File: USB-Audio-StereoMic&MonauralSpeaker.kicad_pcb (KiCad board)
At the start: 2 copper layers, 40 x 40 mm, 39 parts, among them J1 S4B-PH, J2 SJ-2523-SMT-TR, J3 SJ-2523-SMT-TR, J4 S2B-XH-A, J5 SJ2-3593D-SMT-TR, U1 USBLC6-2P6, U2 AP7365-33WG-7, U3 PCM2906CDBR, U4 TPA2006D1DRBR, Y1 12MHz33pF

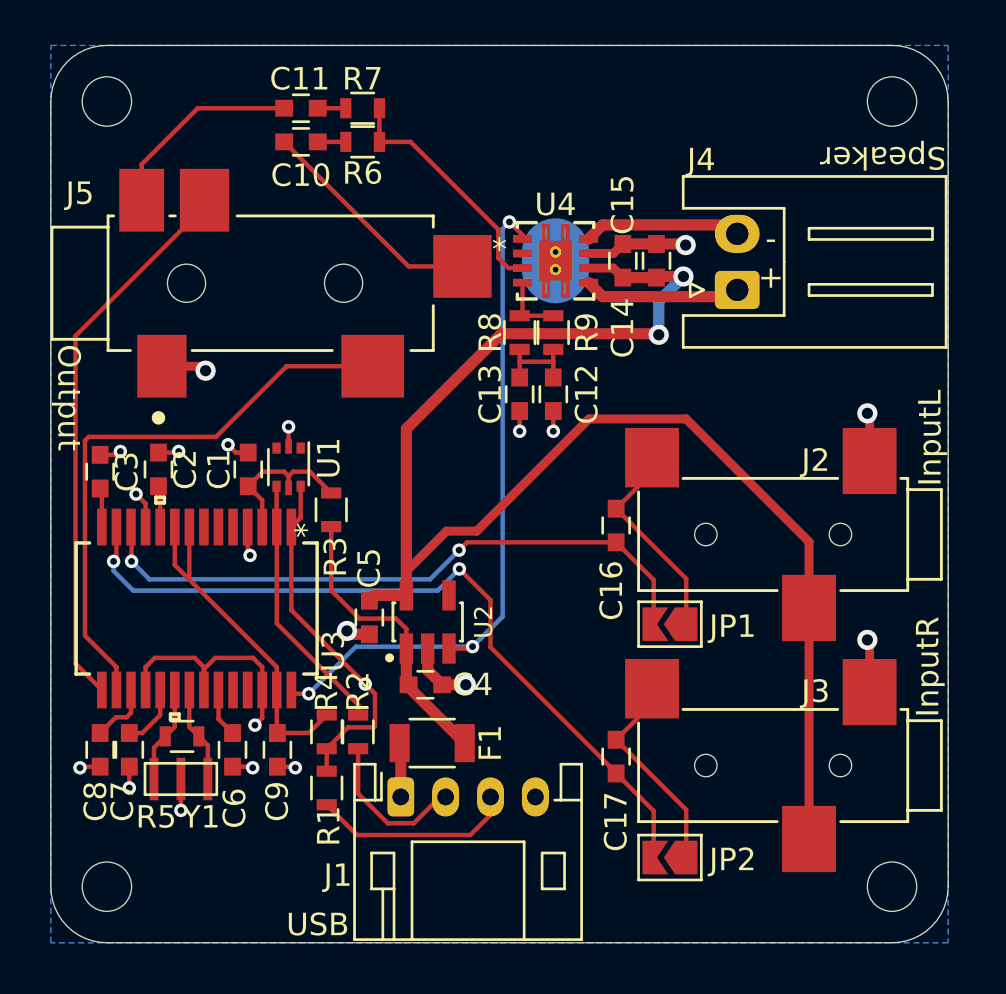
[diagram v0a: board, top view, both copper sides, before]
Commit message: 市販のモノラルマイクに対応
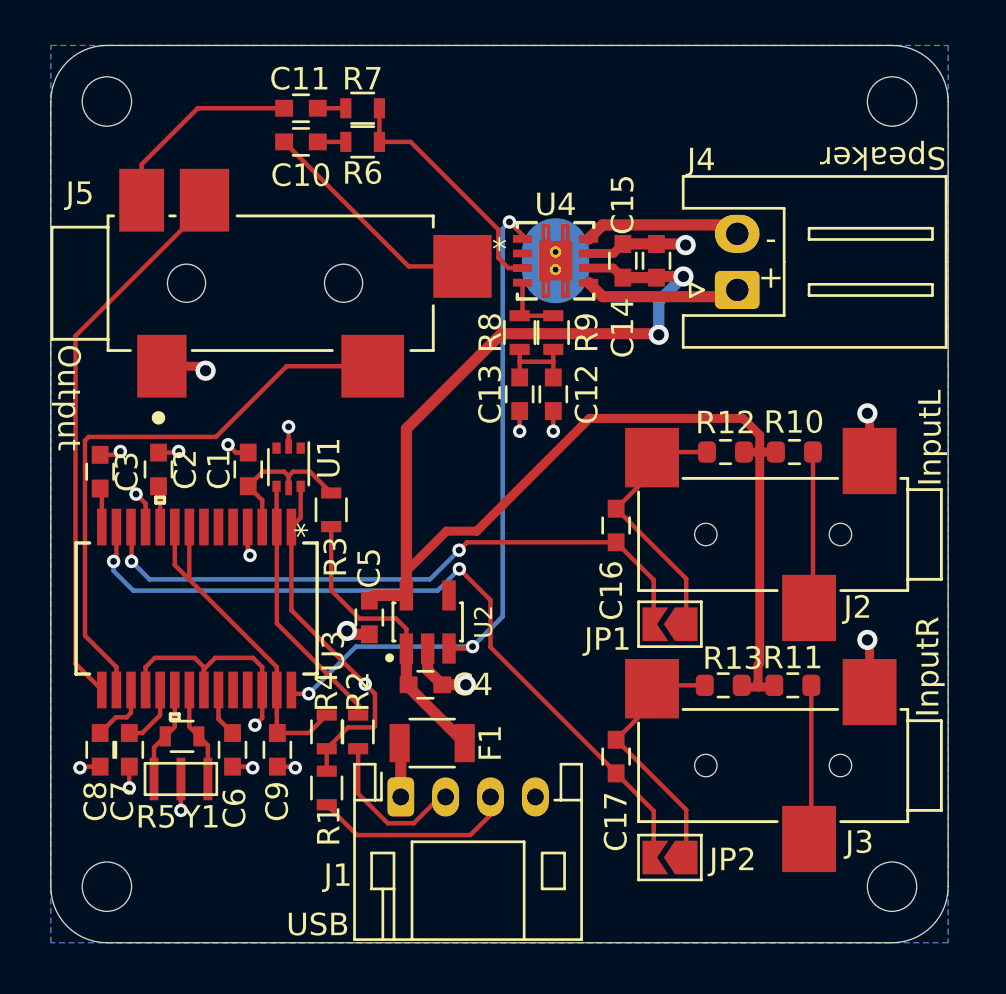
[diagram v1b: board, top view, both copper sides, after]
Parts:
- added R10: 2k, Resistor_SMD:R_0603_1608Metric, F.Cu at (133.2, 113.1)
- added R11: 2k, Resistor_SMD:R_0603_1608Metric, F.Cu at (133.1, 123.5)
- added R12: 2k, Resistor_SMD:R_0603_1608Metric, F.Cu at (130.1, 113.1)
- added R13: 2k, Resistor_SMD:R_0603_1608Metric, F.Cu at (130.0, 123.5)
- JP1, JP2: value Jumper_NO_Small -> JP
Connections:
- J2 pad S: +3V3 -> Net-(J2-PadS)
- J3 pad S: +3V3 -> Net-(J3-PadS)
- U1 pad 1: Net-(U1-Pad1) -> unconnected-(U1-I/O1-Pad1)
- U1 pad 3: Net-(U1-Pad3) -> unconnected-(U1-I/O2-Pad3)
- U2 pad 4: Net-(U2-Pad4) -> unconnected-(U2-NC-Pad4)
- U3 pad 24: Net-(U3-Pad24) -> unconnected-(U3-DIN-Pad24)
- U3 pad 25: Net-(U3-Pad25) -> unconnected-(U3-DOUT-Pad25)
- U3 pad 5: Net-(U3-Pad5) -> unconnected-(U3-HID0-Pad5)
- U3 pad 6: Net-(U3-Pad6) -> unconnected-(U3-HID1-Pad6)
- U3 pad 7: Net-(U3-Pad7) -> unconnected-(U3-HID2-Pad7)
- U4 pad 2: Net-(U4-Pad2) -> unconnected-(U4-NC-Pad2)
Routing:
- net Net-(J3-PadS): track 0.00 -> 7.07 mm
- net Net-(J2-PadS): track 0.00 -> 7.02 mm
- net +3V3: track 67.0 -> 64.0 mm
- net Net-(C16-Pad2): track 9.38 -> 12.0 mm
- net Net-(C17-Pad2): track 9.48 -> 12.0 mm
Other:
- net class Default removed
- board text added: "USB-Audio StereoMic MonauralSpeaker v.1.0 by Nori"
- board text removed: "USB-Audio StereoMic MonauralSpeaker v.0.2 by Nori"
